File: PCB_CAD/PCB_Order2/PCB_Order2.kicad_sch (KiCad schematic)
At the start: 18 parts

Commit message: completed kicad schematic barring only the PSU, supply line filtering, digital RCA and logic level shifters
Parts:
- added C10: 4.7uF, symbol Device:C_Small
- added C11: 220nF, symbol Device:C_Small
- added C9: 2.2uF, symbol Device:C_Small
- added R1: 10k, symbol Device:R_Small_US
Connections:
- net FMC_ALE: now also FLASH.17 (ALE)
- net FMC_CLE: now also FLASH.16 (CLE)
- net FMC_D0: now also FLASH.29 (I/O1)
- net FMC_D1: now also FLASH.30 (I/O2)
- net FMC_D2: now also FLASH.31 (I/O3)
- net FMC_D3: now also FLASH.32 (I/O4)
- net FMC_D4: now also FLASH.41 (I/O5)
- net FMC_D5: now also FLASH.42 (I/O6)
- net FMC_D6: now also FLASH.43 (I/O7)
- net FMC_D7: now also FLASH.44 (I/O8)
- net FMC_NCE: now also FLASH.9 (~{CE})
- net FMC_NOE: now also FLASH.8 (~{RE})
- net FMC_NWAIT: now also FLASH.7 (RY/~{BY})
- net FMC_NWE: now also FLASH.18 (~{WE})
- net GNDA: now also DAC.1 (VSSA)
- net GNDD: now also DAC.12 (LINEGND), FLASH.13 (VSS_1), FLASH.36 (VSS_2), SPDIFTX.21 (DGND), SPDIFTX.23 (MDO/ADR0), SPDIFTX.26 (MS/ADR1), SPDIFTX.27 (MODE), SPDIFTX.45 (RSV1), SPDIFTX.46 (RSV1), C10.2, C9.1
- net VDD: now also DAC.9 (VDDB), FLASH.12 (VCC_1), FLASH.37 (VCC_2), SPDIFTX.22 (DVDD), SPDIFTX.34 (RST), R1.1
- net VDDA: now also DAC.10 (LINEVDD), DAC.2 (VDDA)
- net GND: now reaches AnalogOut.1
- net DAC_ROUT: now reaches AnalogOut.2
- net DAC_ROUT: now also DAC.15 (RLINEOUT)
- net DAC_LOUT: now reaches AnalogOut.3
- net DAC_LOUT: now also DAC.16 (LLINEOU)
- net at DAC.11 (CPCA): now also C11.2
- net at DAC.13 (CPCB): now also C11.1
- net at DAC.14 (CPOUT): now also C10.1
- net at DAC.3 (VREF): now also C9.2
- net at DAC.4 (MUTEB): now also R1.2
- net I2S2_WS: now reaches DAC.5 (FS)
- net I2S2_SDO: now reaches DAC.6 (DACIN)
- net I2S2_SDO: now also uController.27 (PC1)
- net I2S2_CK: now reaches DAC.7 (BCLK)
- net I2S2_MCK: now reaches DAC.8 (MCLK)
- net I2S3_CK: now reaches uController.111 (PC10)
- net I2S3_CK: now also SPDIFTX.8 (MPIO_C1)
- net I2C1_SCL: now reaches uController.136 (PB6)
- net I2C1_SCL: now also SPDIFTX.25 (MC/SCL)
- net I2C1_SDA: now reaches uController.137 (PB7)
- net I2C1_SDA: now also SPDIFTX.24 (MDI/SDA)
- net Flash_WP: now reaches uController.18 (PF6)
- net Flash_WP: now also FLASH.19 (~{WP})
- net I2S3_WS: now reaches uController.40 (PA4)
- net I2S3_WS: now also SPDIFTX.9 (MPIO_C2)
- net I2S3_SDO: now reaches uController.48 (PB2)
- net I2S3_SDO: now also SPDIFTX.10 (MPIO_C3)
- net I2S3_MCK: now reaches uController.97 (PC7)
- net I2S3_MCK: now also SPDIFTX.7 (MPIO_C0)
- net LOGIC SHIFTER: now reaches SPDIFTX.15 (MPO0)
- net ADC_BICK renamed I2S1_CK
- net ADC_LRCLK renamed I2S1_WS
- net ADC_MCLK renamed I2S1_MCK
- net ADC_SDIO renamed I2S1_SDI
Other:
- note added: "Analog In"
- note added: "Analog Out"
- note added: "Digital In"
- note added: "Digital Out"
- note added: "Memory"
- note added: "MicroController"
- moved on the sheet: ADC, AnalogIn, AnalogOut, C1, C2, C3, C4, C5, C6, C7, C8, DAC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

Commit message: added RCA connections, and logic level shifters to kicad schematic
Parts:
- added U1, U2: SN74AXCH1T45DCKR, DCK6_TEX, symbol 2024-10-27_00-26-18:SN74AXCH1T45DCKR
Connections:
- net GNDD: now also DigitalOut.1A (1), U1.2 (GND), U1.5 (DIR), U2.2 (GND)
- net VDD: now also U2.1 (VCCA), U2.5 (DIR)
- net VDDA: now also U1.1 (VCCA)
- net at DigitalIn.2: now also U1.4 (B)
- net at DigitalOut.2: now also U2.4 (B)
- net LOGIC SHIFTER renamed SPDIFTX_OUT
- net SPDIFTX_OUT: now also U2.3 (A)
- new net SPDIFRX_IN0: U1.3 (A)
- new net VDD_DIV: U1.6 (VCCB), U2.6 (VCCB)
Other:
- moved on the sheet: DigitalIn, DigitalOut

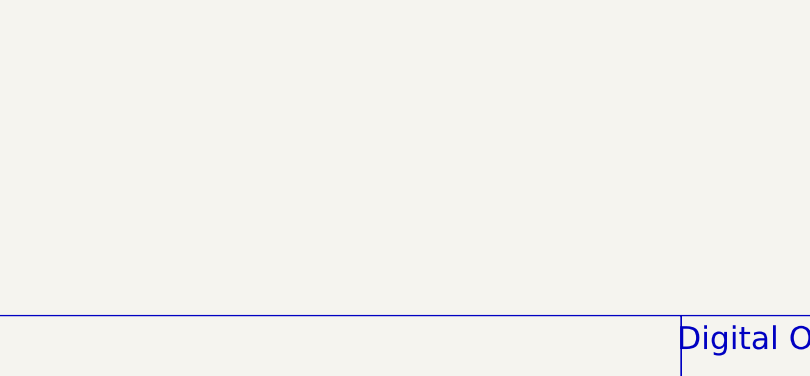
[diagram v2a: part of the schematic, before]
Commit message: added vdd_div voltage divider. Schematic now substantively complete barring noise filtering on power lines and PSU
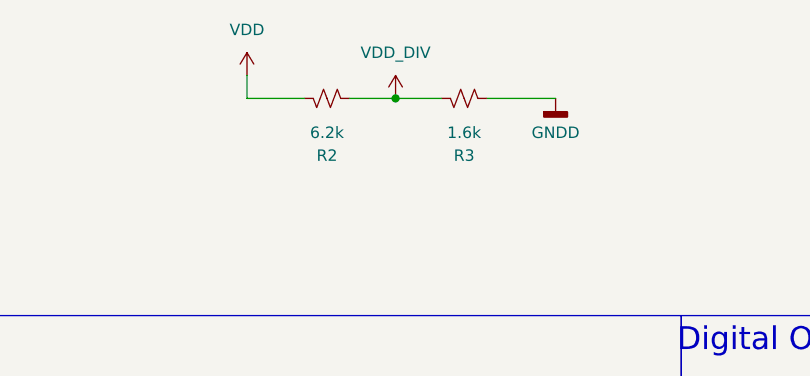
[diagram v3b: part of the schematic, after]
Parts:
- added R2: 6.2k, symbol Device:R_Small_US
- added R3: 1.6k, symbol Device:R_Small_US
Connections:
- net GNDD: now also R3.2
- net VDD: now also R2.1
- net VDD_DIV: now also R2.2, R3.1

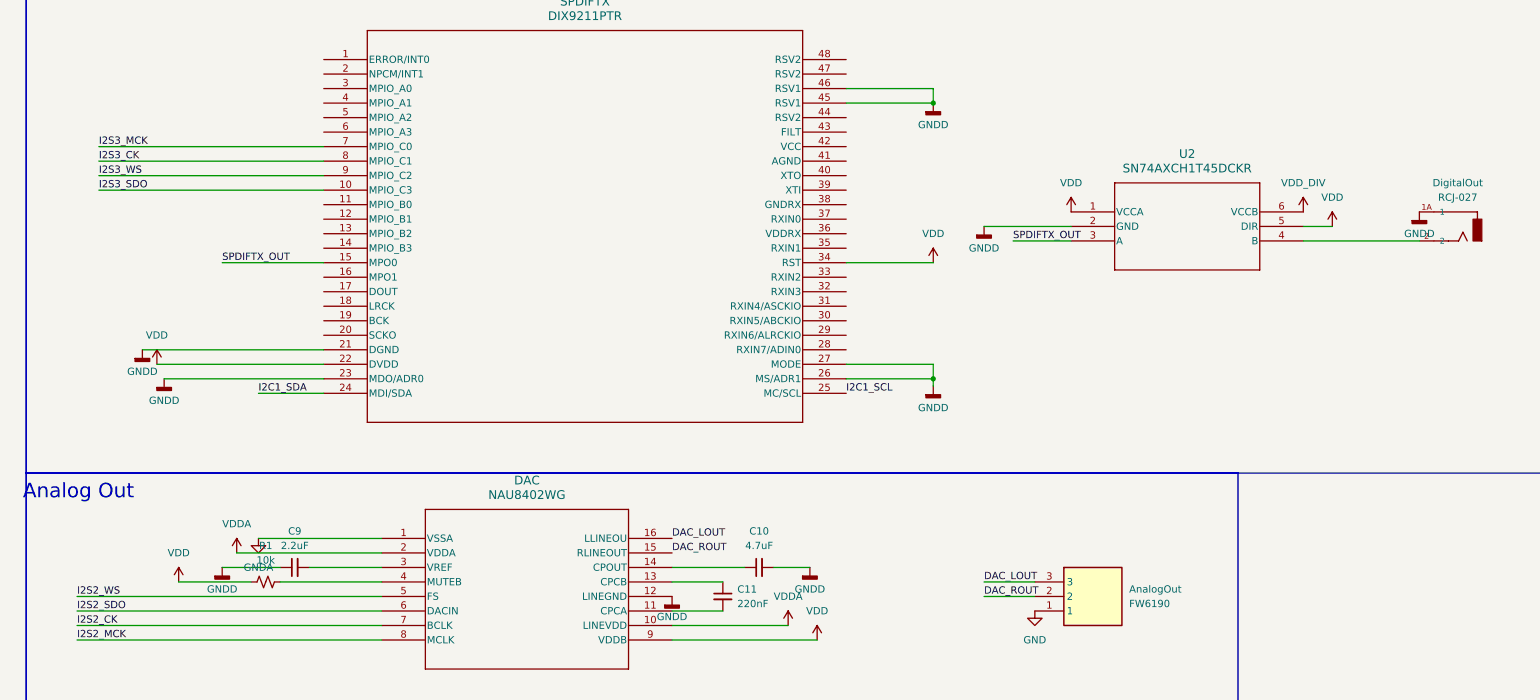
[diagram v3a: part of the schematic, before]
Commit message: power supply decoupling work
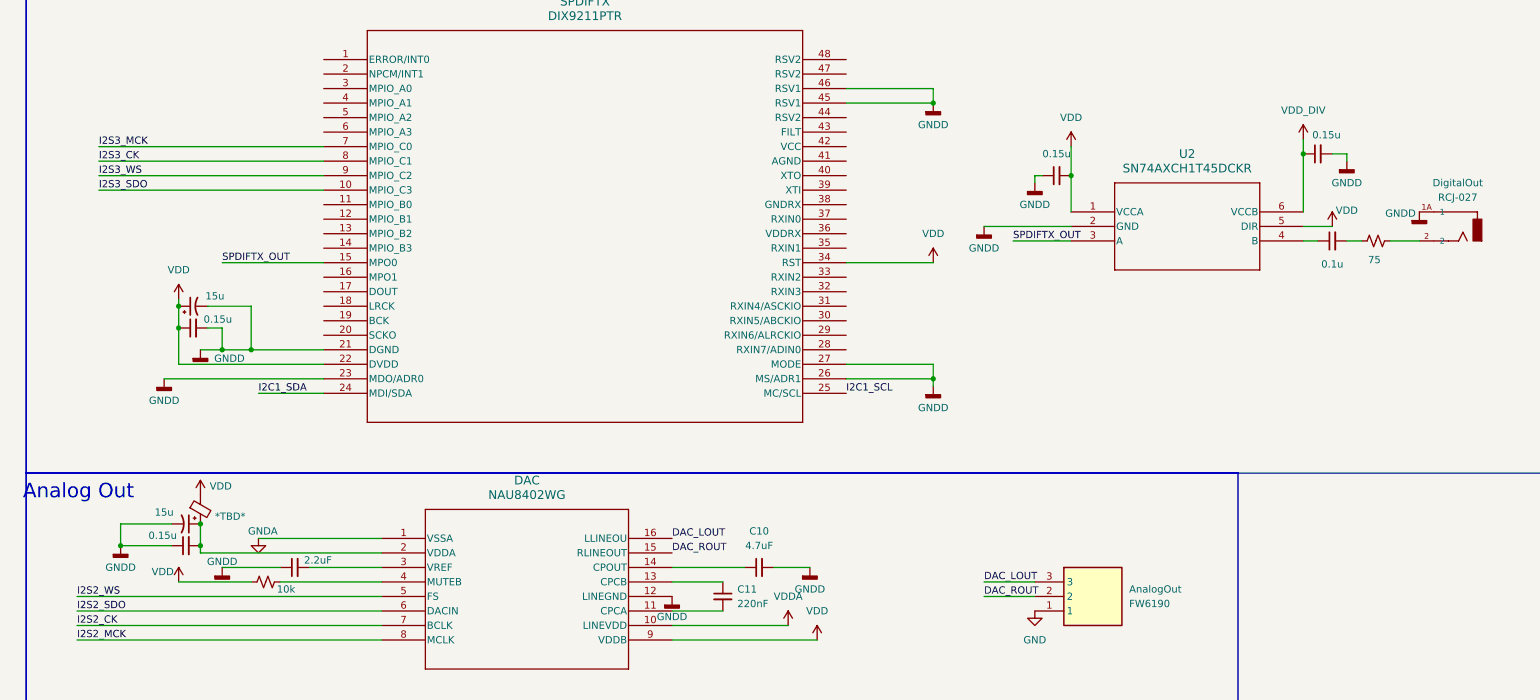
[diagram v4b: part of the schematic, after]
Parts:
- added DacAnalogSupply_bead: *TBD*, symbol Device:FerriteBead_Small
- added DacAnalogSupply_bulk, dixSupply_bulk: 15u, symbol Device:C_Polarized_Small_US
- added DacAnalogSupply_noise, dixSupply_noise, llsOut_refHi_noise, llsOut_refLo_noise: 0.15u, symbol Device:C_Small
- added SpdifOut_AcCoupling: 0.1u, symbol Device:C_Small
- added SpdifOut_ImpedanceMatch: 75, symbol Device:R_Small_US
- renumbered R1 to DacMute_CurrentLimit, C9 to dacVref_bypass
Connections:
- net GNDD: now also DacAnalogSupply_bulk.2, DacAnalogSupply_noise.1, dixSupply_bulk.2, dixSupply_noise.2, llsOut_refHi_noise.1, llsOut_refLo_noise.2
- net VDD: now also DacAnalogSupply_bead.1, dixSupply_bulk.1, dixSupply_noise.1, llsOut_refHi_noise.2
- net VDDA: no longer DAC.2 (VDDA)
- net VDD_DIV: now also llsOut_refLo_noise.1
- net at DigitalOut.2: now also SpdifOut_ImpedanceMatch.2; no longer U2.4 (B)
- new net: DAC.2 (VDDA), DacAnalogSupply_bead.2, DacAnalogSupply_bulk.1, DacAnalogSupply_noise.2
- new net: SpdifOut_AcCoupling.2, SpdifOut_ImpedanceMatch.1
- new net: SpdifOut_AcCoupling.1, U2.4 (B)

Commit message: menial changes to kicad
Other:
- note added: "Analog In (HT CLFRNA)"
- note removed: "Analog In"
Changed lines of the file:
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@@
 		)
 	)
-	(text "Analog In\n\n"
+	(text "Analog In\n(HT CLFRNA)\n"
 		(exclude_from_sim no)
 		(at 206.248 155.194 0)

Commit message: digital in, digital out, analog out complete
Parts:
- added DacOut_L_decouple, DacOut_R_decouple: 2.7n, symbol Device:C_Small
- added DacOut_L_res, DacOut_R_res: 500, symbol Device:R_Small_US
- added Dac_ChargePump_bead: *TBD*, symbol Device:FerriteBead_Small
- added Dac_DigitalSup_bulk, Dac_DigitalSup_bulk1: 15u, symbol Device:C_Polarized_Small_US
- added Dac_DigitalSup_noise, Dac_DigitalSup_noise1, llsOut_refHi_noise1, llsOut_refLo_noise1: 0.15u, symbol Device:C_Small
- added ImpMatching_LLSin: 75, symbol Device:R_Small_US
- added LLSin_ACcouple: 0.1u, symbol Device:C_Small
- renumbered C10 to Dac_ChargePump_Decouple, C11 to Dac_ChargePump_cap
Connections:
- net GND is gone; now on net GNDA: AnalogOut.1
- net GNDA: now also DAC.12 (LINEGND)
- net GNDD: now also DacOut_L_decouple.2, DacOut_R_decouple.2, Dac_DigitalSup_bulk.2, Dac_DigitalSup_bulk1.2, Dac_DigitalSup_noise.2, Dac_DigitalSup_noise1.2, ImpMatching_LLSin.2, llsOut_refHi_noise1.1, llsOut_refLo_noise1.2; no longer DAC.12 (LINEGND)
- net VDD: now also Dac_ChargePump_bead.1, Dac_DigitalSup_bulk.1, Dac_DigitalSup_noise.1
- net VDDA: now also llsOut_refHi_noise1.2; no longer DAC.10 (LINEVDD)
- net VDD_DIV: now also llsOut_refLo_noise1.1
- net at DigitalIn.2: now also ImpMatching_LLSin.1, LLSin_ACcouple.1; no longer U1.4 (B)
- net DAC_LOUT: no longer names the net of AnalogOut.3
- net DAC_LOUT: now also DacOut_L_decouple.1, DacOut_L_res.2; no longer DAC.16 (LLINEOU)
- net DAC_ROUT: no longer names the net of AnalogOut.2
- net DAC_ROUT: now also DacOut_R_decouple.1, DacOut_R_res.2; no longer DAC.15 (RLINEOUT)
- new net: DAC.10 (LINEVDD), Dac_ChargePump_bead.2, Dac_DigitalSup_bulk1.1, Dac_DigitalSup_noise1.1
- new net: DAC.15 (RLINEOUT), DacOut_R_res.1
- new net: LLSin_ACcouple.2, U1.4 (B)
- new net: DAC.16 (LLINEOU), DacOut_L_res.1
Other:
- moved on the sheet: AnalogOut

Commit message: latched footprints to each symbol in the kicad schematic
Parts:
- AnalogIn1: renamed from AnalogIn; footprint FW6190 -> CustomModels:FW6190
- AnalogOut1: renamed from AnalogOut; footprint FW6190 -> CustomModels:FW6190
- C1, C2, C3, C4, C6, C8, Dac_DigitalSup_bulk1, Dac_DigitalSup_noise1, llsOut_refHi_noise1, llsOut_refLo_noise1: footprint (none) -> Capacitor_SMD:C_0805_2012Metric_Pad1.18x1.45mm_HandSolder
- C5, C7: footprint Capacitor_SMD:CP_Elec_3x5.3 -> Capacitor_SMD:C_0805_2012Metric_Pad1.18x1.45mm_HandSolder
- DAC1: renamed from DAC; footprint TSSOP16_NAU8402_NUV -> CustomModels:TSSOP16_NAU8402_NUV
- DacAnalogSupply_bead1: renamed from DacAnalogSupply_bead; footprint (none) -> Resistor_SMD:R_0603_1608Metric
- DacAnalogSupply_bulk1: renamed from DacAnalogSupply_bulk; footprint (none) -> Capacitor_SMD:C_0805_2012Metric_Pad1.18x1.45mm_HandSolder
- DacAnalogSupply_noise1: renamed from DacAnalogSupply_noise; footprint (none) -> Capacitor_SMD:C_0805_2012Metric_Pad1.18x1.45mm_HandSolder
- DacMute_CurrentLimit1: renamed from DacMute_CurrentLimit; footprint (none) -> Resistor_SMD:R_0603_1608Metric_Pad0.98x0.95mm_HandSolder
- DacOut_L_decouple1: renamed from DacOut_L_decouple; footprint (none) -> Capacitor_SMD:C_0805_2012Metric_Pad1.18x1.45mm_HandSolder
- DacOut_L_res1: renamed from DacOut_L_res; footprint (none) -> Resistor_SMD:R_0603_1608Metric_Pad0.98x0.95mm_HandSolder
- DacOut_R_decouple1: renamed from DacOut_R_decouple; footprint (none) -> Capacitor_SMD:C_0805_2012Metric_Pad1.18x1.45mm_HandSolder
- DacOut_R_res1: renamed from DacOut_R_res; footprint (none) -> Resistor_SMD:R_0603_1608Metric_Pad0.98x0.95mm_HandSolder
- Dac_ChargePump_Decouple1: renamed from Dac_ChargePump_Decouple; footprint (none) -> Capacitor_SMD:C_0805_2012Metric_Pad1.18x1.45mm_HandSolder
- Dac_ChargePump_bead1: renamed from Dac_ChargePump_bead; footprint (none) -> Resistor_SMD:R_0603_1608Metric
- Dac_ChargePump_cap1: renamed from Dac_ChargePump_cap; footprint (none) -> Capacitor_SMD:C_0805_2012Metric_Pad1.18x1.45mm_HandSolder
- Dac_DigitalSup_bulk2: renamed from Dac_DigitalSup_bulk; footprint (none) -> Capacitor_SMD:C_0805_2012Metric_Pad1.18x1.45mm_HandSolder
- Dac_DigitalSup_noise2: renamed from Dac_DigitalSup_noise; footprint (none) -> Capacitor_SMD:C_0805_2012Metric_Pad1.18x1.45mm_HandSolder
- DigitalIn1: renamed from DigitalIn; footprint RCJ-027:CUI_RCJ-027 -> CustomModels:CUI_RCJ-027
- DigitalOut1: renamed from DigitalOut; footprint RCJ-027:CUI_RCJ-027 -> CustomModels:CUI_RCJ-027
- FLASH1: renamed from FLASH; footprint SOP50P2000X120-48N -> KiCad:SOP50P2000X120-48N
- ImpMatching_LLSin1: renamed from ImpMatching_LLSin; footprint (none) -> Resistor_SMD:R_0603_1608Metric
- LLSin_ACcouple1: renamed from LLSin_ACcouple; footprint (none) -> Capacitor_SMD:C_0805_2012Metric_Pad1.18x1.45mm_HandSolder
- R2, R3: footprint (none) -> Resistor_SMD:R_0603_1608Metric
- RAM1: renamed from RAM; footprint SOP80P1176X120-54N -> CustomModels:SOP80P1176X120-54N
- SPDIFTX1: renamed from SPDIFTX; footprint PT48 -> CustomModels:DIX9211PTR
- SpdifOut_AcCoupling1: renamed from SpdifOut_AcCoupling; footprint (none) -> Capacitor_SMD:C_0805_2012Metric_Pad1.18x1.45mm_HandSolder
- SpdifOut_ImpedanceMatch1: renamed from SpdifOut_ImpedanceMatch; footprint (none) -> Resistor_SMD:R_0603_1608Metric
- U1, U2: footprint DCK6_TEX -> CustomModels:DCK6_TEX
- dacVref_bypass1: renamed from dacVref_bypass; footprint (none) -> Capacitor_SMD:C_0805_2012Metric_Pad1.18x1.45mm_HandSolder
- dixSupply_bulk1: renamed from dixSupply_bulk; footprint (none) -> Capacitor_SMD:C_0805_2012Metric_Pad1.18x1.45mm_HandSolder
- dixSupply_noise1: renamed from dixSupply_noise; footprint (none) -> Capacitor_SMD:C_0805_2012Metric_Pad1.18x1.45mm_HandSolder
- llsOut_refHi_noise2: renamed from llsOut_refHi_noise; footprint (none) -> Capacitor_SMD:C_0805_2012Metric_Pad1.18x1.45mm_HandSolder
- llsOut_refLo_noise2: renamed from llsOut_refLo_noise; footprint (none) -> Capacitor_SMD:C_0805_2012Metric_Pad1.18x1.45mm_HandSolder
- renumbered ADC to ADC1, uController to uController1
